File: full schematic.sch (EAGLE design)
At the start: 70 parts, among them U1 ATMEGA328P-AU, U2 FT231XS

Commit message: updated board with more components
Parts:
- removed C14, C27, C28, C29: 10uF, SparkFun-Retired:.22UF-CER
- removed C16, C17: 4.7pF, SparkFun-Retired:.22UF-CER
- removed C18, C19: .22uF, SparkFun-Retired:.22UF-CER
- removed C20, C21, C22, C23, C24: .1uF, SparkFun-Retired:.22UF-CER
- removed C25: 1uF, SparkFun-Retired:.22UF-CER
- removed C26: 1nF, SparkFun-Retired:.22UF-CER
- removed C30: 10uF, SparkFun-Retired:10UF-TANT
- removed C31, C32: 47pF, SparkFun-Retired:.22UF-CER
- removed J1: (no value), SparkFun-Connectors:USB_MICRO-B_SMT
- removed R14, R16, R17: 22k, SparkFun-Resistors:0.05OHM-0603-1/5W-1%
- removed R18, R19, R27, R28, R30, R31: 27, SparkFun-Resistors:0.05OHM-0603-1/5W-1%
- removed R20, R29: 2M, SparkFun-Resistors:0.05OHM-0603-1/5W-1%
- removed R21, R22, R23, R24, R25, R26: 10k, SparkFun-Resistors:0.05OHM-0603-1/5W-1%
- removed R32, R33: 1k, SparkFun-Resistors:0.05OHM-0603-1/5W-1%
- removed U2: FT231XS, SparkFun-IC-Comms:FT231XS
- added ATMEGA328P-AU: ATMEGA328P-AU, Atmega-328pu:ATMEGA328P-AU
- added BUZZER: BUZZER-PTH, SparkFun-Electromechanical:BUZZER-PTH
- added D1, D2, D3, D4: LED-IRTSAL6100, SparkFun-LED:LED-IRTSAL6100
- added D5: 700mA/40V/533mV, SparkFun-DiscreteSemi:DIODE-SCHOTTKY-ZLLS500
- added FTDI231XS1: FT231XS, SparkFun-IC-Comms:FT231XS
- added IC1, IC2: (no value), linear-technology:LT1129CST5
- added J2: (no value), SparkFun-Connectors:USB_MICRO-B_SMT
- added J3, J4, J5, J6, J7_TMP, J7_TMP1, J7_TMP2, J8_TMP, J8_TMP1: (no value), SparkFun-Connectors:CONN_02LOCK
- added J7_5V_BACKUP: (no value), SparkFun-Connectors:CONN_01
- added J7_NEO, J8_NEO: (no value), SparkFun-Connectors:CONN_03-SCREW-5MM
- added JP1: JUMPER-SMT_2_NO_NO-SILK_ROUND, SparkFun-Jumpers:JUMPER-SMT_2_NO_NO-SILK_ROUND
- added MPU6050: MPU-6050, KevinKuwata1:MPU-6050
- added Q1: NPN 40V 1A SOT-23, semicon-smd-ipc:NPN-TRANSISTOR_SOT23
- added Q2: (no value), semicon-smd-ipc:NPN-TRANSISTOR_SOT23
- added TMP36: (no value), SparkFun-Sensors:TMP36GT9
- added U$1: 1N7002PW, KevinKuwata1:1N7002PW
- C1, C2: value .22uF -> .1uF
- C10: value 1uF -> 47pF
- C11: value 1nF -> 10uF; device SparkFun-Retired:.22UF-CER -> SparkFun-Retired:10UF-TANT
- C12, C13: device SparkFun-Retired:.22UF-CER -> SparkFun-Retired:10UF-TANT
- C15: value 10uF -> 47uF; device SparkFun-Retired:.22UF-CER -> SparkFun-Retired:10UF-TANT
- C3: value .1uF -> 10nF
- C4: value .1uF -> 2.2nF
- C6: value .1uF -> 47pF
- R13: value 1k -> PHOTOCELLPTH-KIT; device SparkFun-Resistors:0.05OHM-0603-1/5W-1% -> SparkFun-Sensors:PHOTOCELLPTH-KIT
- R15: value 22k -> 1k
- R5, R7: value 10k -> 27
- U1: value ATMEGA328P-AU -> WS2812; device Atmega-328pu:ATMEGA328P-AU -> SparkFun-LED:WS2812"
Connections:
- removed net 13: U1.PB5
- removed net A4: U1.PC4
- removed net A5: C7.2, U1.PC5
- removed net D0: U1.PD0
- removed net D1: U1.PD1
- removed net D10: U1.PB2
- removed net D11: U1.PB3
- removed net D12: U1.PB4
- removed net N$10: R31.2, U2.USBDP
- removed net N$11: R30.2, U2.USBDM
- removed net N$12: C30.+, U2.VCC
- removed net N$8: C31.1, J1.D+, R30.1
- removed net N$9: C32.1, J1.D-, R31.1
- new net 3.3VFTDI: C1.1, FTDI231XS1.!RESET, FTDI231XS1.3V3OUT, FTDI231XS1.VCCIO, R3.2, U$1.G
- new net ADO: MPU6050.AD0
- new net BUZ+: BUZZER.1, J7_TMP2.1, J8_TMP1.1, R10.1
- new net BUZ-: BUZZER.2, J7_TMP2.2, J8_TMP1.2, Q2.C, R10.2
- new net GND: J3.1, J4.1, J7_NEO.3, R13.P$1, U1.VSS
- new net INT: MPU6050.INT
- new net IR_-: D4.C, J5.2, J6.2, Q1.C
- new net IR_LED: Q1.B, R15.1
- new net MISO: ATMEGA328P-AU.PB4
- new net MOSI: ATMEGA328P-AU.PB3
- new net N$13: C10.1, J2.D-, R7.1
- new net N$15: FTDI231XS1.USBDM, R5.2
- new net N$16: C11.+, FTDI231XS1.VCC
- new net N$18: D1.C, D2.A
- new net N$19: D2.C, D3.A
- new net N$20: Q2.B, R11.1
- new net N$21: D3.C, D4.A
- new net N$22: D5.A, J7_TMP1.1
- new net N$23: C12.+, IC1G$1.OUT, J7_5V_BACKUP.1, JP1.2
- new net RXLED: FTDI231XS1.CBUS1
- new net SCK: ATMEGA328P-AU.PB5
- new net SCL: ATMEGA328P-AU.PC4, MPU6050.SLC, R2.2
- new net SDA: ATMEGA328P-AU.PC5, C7.2, MPU6050.SDA, R1.2
- new net SS: ATMEGA328P-AU.PB2
- new net TMP+: J7_TMP.1, J8_TMP.1, TMP36.VCC
- new net TMP-: J7_TMP.2, J8_TMP.2, TMP36.GND
- new net TXLED: FTDI231XS1.CBUS2
- new net VCC: C13.+, IC2G$1.OUT
- new net VIN: C15.+, D5.C, IC1G$1.IN
- net 3.3V: now also ATMEGA328P-AU.GND, ATMEGA328P-AU.GND_2, ATMEGA328P-AU.GND_3, C1.2, C10.2, C11.-, C12.-, C13.-, C15.-, C2.2, C3.2, C4.2, C5.2, C6.2, C8.2, FTDI231XS1.GND@16, FTDI231XS1.GND@6, IC1G$1.GND, IC2G$1.GND, J2.GND, J7_TMP1.2, J8_NEO.3, MPU6050.GND, Q1.E, Q2.E; no longer C22.2, C23.2, C30.-, C31.2, C32.2, J1.GND, U1.GND, U1.GND_2, U1.GND_3, U2.GND@16, U2.GND@6
- net 5V: now also ATMEGA328P-AU.AVCC, ATMEGA328P-AU.VCC, ATMEGA328P-AU.VCC_2, C2.1, C5.1, D1.A, IC2G$1.IN, J2.VBUS, J5.1, J6.1, J7_NEO.1, J8_NEO.2, JP1.1, MPU6050.VDD, R1.1, R12.1, R2.1, R4.1, U$1.D, U1.DI; no longer C23.1, J1.VBUS, U1.AVCC, U1.VCC, U1.VCC_2
- net A0: now also ATMEGA328P-AU.PC0, J3.2, J4.2, R12.2, R13.P$2; no longer U1.PC0
- net A1: now also ATMEGA328P-AU.PC1, TMP36.VOUT; no longer U1.PC1
- net A2: now also ATMEGA328P-AU.PC2; no longer U1.PC2
- net A3: now also ATMEGA328P-AU.PC3; no longer U1.PC3
- net A6: now also ATMEGA328P-AU.ADC6; no longer U1.ADC6
- net A7: now also ATMEGA328P-AU.ADC7; no longer U1.ADC7
- net D2: now also ATMEGA328P-AU.PD2; no longer U1.PD2
- net D3: now also ATMEGA328P-AU.PD3, R11.2; no longer U1.PD3
- net D4: now also ATMEGA328P-AU.PD4; no longer U1.PD4
- net D5: now also ATMEGA328P-AU.PD5; no longer U1.PD5
- net D6: now also ATMEGA328P-AU.PD6; no longer U1.PD6
- net D7: now also ATMEGA328P-AU.PD7, R15.2; no longer U1.PD7
- net D8: now also ATMEGA328P-AU.PB0; no longer U1.PB0
- net D9: now also ATMEGA328P-AU.PB1, J7_NEO.2, J8_NEO.1, U1.VDD; no longer U1.PB1
- net DTR: now also R4.2
- net DTR_FTDI: now also FTDI231XS1.!DTR, R3.1, U$1.S; no longer R22.1, U2.!DTR
- net N$1: now also ATMEGA328P-AU.PB6; no longer U1.PB6
- net N$14: now also FTDI231XS1.USBDP, R7.2; no longer C22.1, U2.!RESET
- net N$2: now also ATMEGA328P-AU.PB7; no longer U1.PB7
- net N$3: now also C4.1, MPU6050.CPOUT; no longer R3.2, R4.1
- net N$4: now also C8.1, MPU6050.REGOUT; no longer R4.2, R5.1
- net N$5: now also C3.1, MPU6050.VLOG; no longer R23.2, R24.1
- net N$6: now also ATMEGA328P-AU.AREF; no longer U1.AREF
- net N$7: now also C6.1, J2.D+, R5.1; no longer R24.2, R25.1
- net RESET: now also ATMEGA328P-AU.PC6; no longer U1.PC6
- net RX: now also FTDI231XS1.RXD, R9.1; no longer R33.1, U2.RXD
- net RX-I: now also ATMEGA328P-AU.PD0, R8.2; no longer R32.2
- net TX: now also FTDI231XS1.TXD, R8.1; no longer R32.1, U2.TXD
- net TX-O: now also ATMEGA328P-AU.PD1, R9.2; no longer R33.2

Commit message: sd card added
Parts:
- added U$2: WM6698TR-ND_MICROSD, KevinKuwata1:WM6698TR-ND_MICROSD
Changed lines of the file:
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@@
 <part name="J7_TMP2" library="SparkFun-Connectors" deviceset="CONN_02" device="LOCK"/>
 <part name="U$1" library="KevinKuwata1" deviceset="1N7002PW" device=""/>
+<part name="U$2" library="KevinKuwata1" deviceset="WM6698TR-ND_MICROSD" device=""/>
 </parts>
 <sheets>
@@
 <instance part="J7_TMP2" gate="G$1" x="-201.93" y="180.34" rot="MR180"/>
 <instance part="U$1" gate="G$1" x="-91.44" y="53.34" rot="R270"/>
+<instance part="U$2" gate="G1" x="168.91" y="153.67"/>
 </instances>
 <busses>

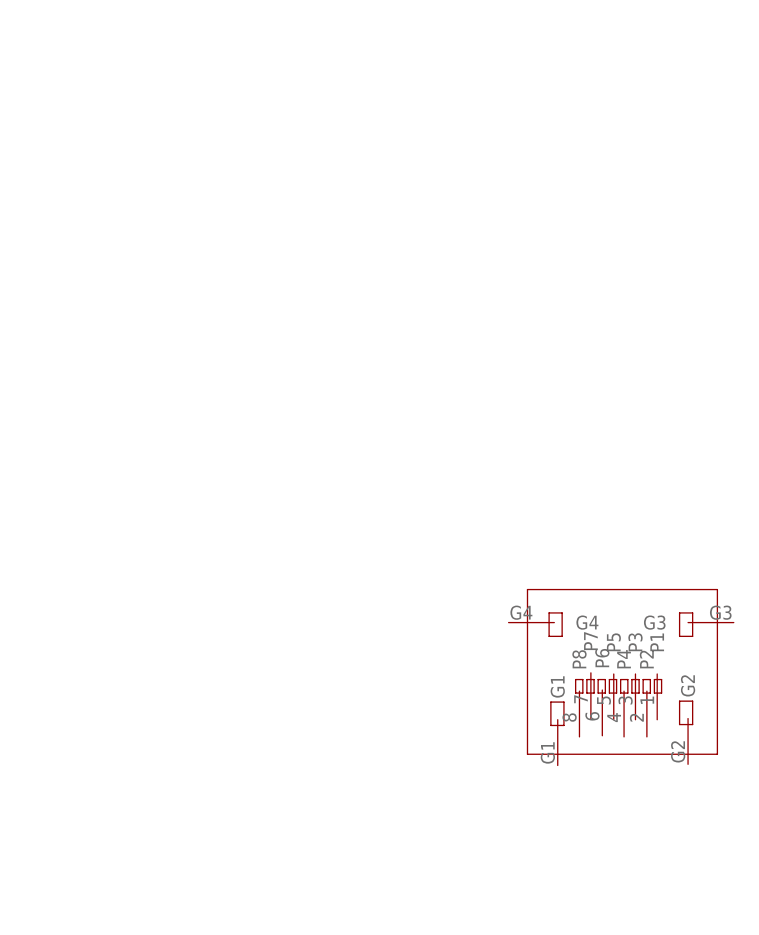
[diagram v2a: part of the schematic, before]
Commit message: sd card fully laid out
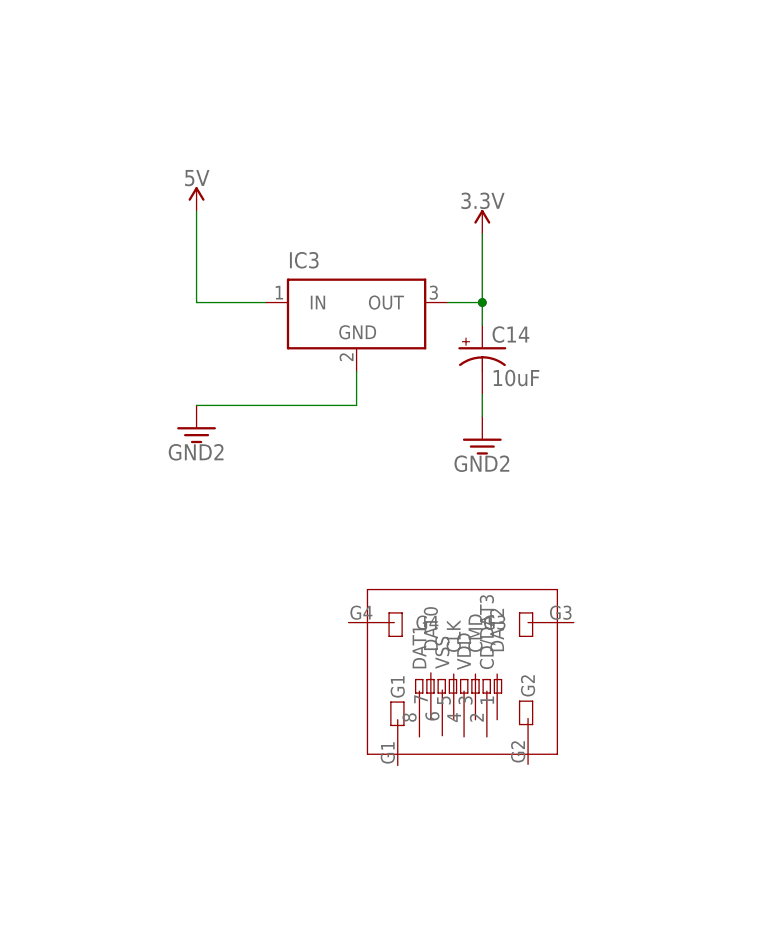
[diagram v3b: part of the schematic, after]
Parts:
- added C14: 10uF, SparkFun-Retired:10UF-TANT
- added IC3: (no value), linear-technology:LT1129CST5
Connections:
- net 3.3V: now also C14.-, IC3G$1.GND
- net 5V: now also IC3G$1.IN
- net VCC: now also C14.+, IC3G$1.OUT
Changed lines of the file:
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@@
 <part name="U$1" library="KevinKuwata1" deviceset="1N7002PW" device=""/>
 <part name="U$2" library="KevinKuwata1" deviceset="WM6698TR-ND_MICROSD" device=""/>
+<part name="SUPPLY17" library="SparkFun-PowerSymbols" deviceset="5V" device=""/>
+<part name="GND9" library="SparkFun-PowerSymbols" deviceset="GND2" device=""/>
+<part name="GND10" library="SparkFun-PowerSymbols" deviceset="GND2" device=""/>
+<part name="C14" library="SparkFun-Retired" deviceset="10UF-TANT" device="" value="10uF"/>
+<part name="IC3" library="linear-technology" deviceset="LT1129CST5" device=""/>
+<part name="SUPPLY18" library="SparkFun-PowerSymbols" deviceset="VCC" device="" value="3.3V"/>
 </parts>
 <sheets>
@@
 <instance part="J7_TMP2" gate="G$1" x="-201.93" y="180.34" rot="MR180"/>
 <instance part="U$1" gate="G$1" x="-91.44" y="53.34" rot="R270"/>
-<instance part="U$2" gate="G1" x="168.91" y="153.67"/>
+<instance part="U$2" gate="G1" x="151.13" y="153.67"/>
+<instance part="SUPPLY17" gate="G$1" x="129.54" y="210.82"/>
+<instance part="GND9" gate="G$1" x="129.54" y="186.69"/>
+<instance part="GND10" gate="G$1" x="161.29" y="185.42"/>
+<instance part="C14" gate="G$1" x="161.29" y="195.58"/>
+<instance part="IC3" gate="G$1" x="147.32" y="198.12"/>
+<instance part="SUPPLY18" gate="G$1" x="161.29" y="208.28"/>
 </instances>
 <busses>
@@
 <wire x1="-95.25" y1="-27.94" x2="-95.25" y2="-30.48" width="0.1524" layer="91"/>
 </segment>
+<segment>
+<pinref part="GND9" gate="G$1" pin="3.3V"/>
+<wire x1="129.54" y1="189.23" x2="147.32" y2="189.23" width="0.1524" layer="91"/>
+<pinref part="IC3" gate="G$1" pin="GND"/>
+<wire x1="147.32" y1="189.23" x2="147.32" y2="193.04" width="0.1524" layer="91"/>
+</segment>
+<segment>
+<pinref part="C14" gate="G$1" pin="-"/>
+<pinref part="GND10" gate="G$1" pin="3.3V"/>
+<wire x1="161.29" y1="190.5" x2="161.29" y2="187.96" width="0.1524" layer="91"/>
+</segment>
 </net>
 <net name="N$6" class="0">
@@
 <pinref part="IC2" gate="G$1" pin="IN"/>
 <wire x1="-119.38" y1="-17.78" x2="-127" y2="-17.78" width="0.1524" layer="91"/>
+</segment>
+<segment>
+<pinref part="SUPPLY17" gate="G$1" pin="5V"/>
+<wire x1="129.54" y1="210.82" x2="129.54" y2="200.66" width="0.1524" layer="91"/>
+<pinref part="IC3" gate="G$1" pin="IN"/>
+<wire x1="137.16" y1="200.66" x2="129.54" y2="200.66" width="0.1524" layer="91"/>
 </segment>
 </net>
@@
 <junction x="-95.25" y="-17.78"/>
 </segment>
-</net>
+<segment>
+<pinref part="IC3" gate="G$1" pin="OUT"/>
+<wire x1="157.48" y1="200.66" x2="161.29" y2="200.66" width="0.1524" layer="91"/>
+<pinref part="C14" gate="G$1" pin="+"/>
+<wire x1="161.29" y1="200.66" x2="161.29" y2="198.12" width="0.1524" layer="91"/>
+<pinref part="SUPPLY18" gate="G$1" pin="VCC"/>
+<wire x1="161.29" y1="208.28" x2="161.29" y2="200.66" width="0.1524" layer="91"/>
+<junction x="161.29" y="200.66"/>
+</segment>
+</net>
